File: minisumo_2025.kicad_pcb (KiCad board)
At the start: 4 copper layers, 62.4 x 98 mm, 139 parts, among them J1 USB_C Connector, J10 DISTANCE_R90, J11 DISTANCE_R, J12 DISTANCE_RF, J13 DISTANCE_L90, J14 DISTANCE_L, J15 LINE_LEFT, J16 DISTANCE_LF, J3 START_MODULE, J4 MOTOR1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

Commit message: routing
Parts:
- removed the C10 at (129.6, 46.6)
- removed the C10 at (161.6, 39.9)
- removed the C11 at (129.0, 55.9)
- removed the C11 at (162.3, 49.5)
- removed the C13 at (157.7, 59.7)
- removed the C13 at (123.5, 66.2)
- removed the C3 at (159.8, 58.8)
- removed the C3 at (126.0, 65.3)
- removed the C4 at (156.9, 46.6)
- removed the C4 at (124.8, 53.2)
- removed the C5 at (159.1, 49.5)
- removed the C5 at (125.3, 55.9)
- removed the C8 at (161.6, 43.2)
- removed the C8 at (129.6, 53.2)
- removed the C9 at (161.6, 46.7)
- removed the C9 at (129.6, 49.9)
- removed the L1 at (130.7, 61.0)
- removed the L1 at (165.3, 55.0)
- removed the R4 at (119.1, 62.7)
- removed the R4 at (154.0, 56.5)
- removed the R5 at (120.7, 62.8)
- removed the R5 at (155.1, 56.5)
- removed the U1 at (124.2, 61.0)
- removed the U1 at (158.4, 54.3)
- added C10: 47uF, Capacitor_SMD:C_1210_3225Metric, F.Cu at (125.4, 47.6)
- added C11: 100nF, Capacitor_SMD:C_0603_1608Metric, F.Cu at (126.4, 57.1)
- added C13: 1uF, Capacitor_SMD:C_0603_1608Metric, F.Cu at (121.7, 67.2)
- added C3: 0.1uF, Capacitor_SMD:C_0603_1608Metric, F.Cu at (124.0, 66.5)
- added C4: 10uF, Capacitor_SMD:C_1210_3225Metric, F.Cu at (120.7, 54.3)
- added C5: 220nF, Capacitor_SMD:C_0805_2012Metric, F.Cu at (123.1, 57.2)
- added C8: 47uF, Capacitor_SMD:C_1210_3225Metric, F.Cu at (125.4, 54.3)
- added C9: 47uF, Capacitor_SMD:C_1210_3225Metric, F.Cu at (125.4, 50.9)
- added L1: 10uH, 27mOhm, footprints:IND_XAL6060-103MEC, F.Cu at (129.1, 62.5)
- added R4: 100k, Resistor_SMD:R_0603_1608Metric, F.Cu at (117.2, 63.9)
- added R5: 22.1k, Resistor_SMD:R_0603_1608Metric, F.Cu at (118.7, 63.9)
- added U1: LMR33630ADDAR, footprints:DDA0008J, F.Cu at (122.3, 62.0)
- TP13: value GPIO48 -> GPIO17
- moved D2 79.0 mm to (109.7, 124.3)
- moved R6 78.8 mm to (113.8, 124.2)
- moved D1 18.5 mm to (131.9, 47.3), turned to 180 degrees
- moved R22 10.8 mm to (115.1, 70.2), turned to 90 degrees
- moved C15 9.33 mm to (118.4, 47.4), turned to -90 degrees
- moved R23 8.91 mm to (117.0, 120.2), turned to 90 degrees
- moved R24 8.87 mm to (117.2, 117.1), turned to 90 degrees
- moved R2 7.85 mm to (159.6, 76.2)
- moved R32 6.78 mm to (115.5, 120.2), turned to -90 degrees
- moved R21 6.74 mm to (115.1, 67.2), turned to 90 degrees
- moved D18 6.53 mm to (115.5, 117.1), turned to -90 degrees
- moved U4 3.65 mm to (115.4, 47.2), turned to 180 degrees
- moved C14 2.49 mm to (112.4, 47.4), turned to -90 degrees
- moved D17 0.98 mm to (109.5, 65.1)
- moved R31 0.98 mm to (112.5, 65.1)
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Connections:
- J8 pad 3: /GPIO12 -> /GPIO48
- J8 pad 4: /GPIO11 -> /GPIO47
- J8 pad 5: /GPIO10 -> /GPIO21
- R19 pad 1: /GPIO14 -> /GPIO38
- TP13 pad 1: /GPIO48 -> /GPIO17
- U3 pad 17: /DISTANCE_INTR -> /GPIO9
- U3 pad 22: /GPIO14 -> /DISTANCE_INTR
- U3 pad 4: /DISTANCE_L90 -> /DISTANCE_R90
- U3 pad 5: /DISTANCE_L -> /DISTANCE_R
- U3 pad 6: /DISTANCE_LF -> /DISTANCE_RF
- U3 pad 7: /DISTANCE_RF -> /DISTANCE_LF
- U3 pad 8: /DISTANCE_R -> /DISTANCE_L
- U3 pad 9: /DISTANCE_R90 -> /DISTANCE_L90
- U6 pad 1: /GPIO17 -> /GPIO10
- U6 pad 2: /GPIO21 -> /GPIO9
- U7 pad 1: /GPIO47 -> /GPIO12
- U7 pad 2: /GPIO38 -> /GPIO11
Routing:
- net /GPIO48: track 0.00 -> 40.3 mm
- net /GPIO21: track 11.7 -> 44.2 mm
- net /GPIO10: track 43.0 -> 14.1 mm
- net /GPIO47: track 18.2 -> 42.4 mm
- net /GPIO11: track 41.2 -> 19.6 mm
- net /GPIO12: track 39.2 -> 19.6 mm
- net /GPIO9: track 0.00 -> 12.8 mm
- net /GPIO17: track 12.7 -> 25.3 mm, vias 0 -> 2
- net /INV_2: track 50.9 -> 38.5 mm
- net /GPIO18: track 56.4 -> 45.7 mm
- net GND: track 21.7 -> 29.3 mm, vias 56 -> 95
- net +5V: track 8.18 -> 12.3 mm, vias 0 -> 2
- net /GPIO8: track 49.6 -> 52.8 mm
- net /DISTANCE_R: track 30.9 -> 33.2 mm
- net /DISTANCE_R90: track 33.0 -> 34.9 mm
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- added copper zone on In2.Cu, net +3V3
- added copper zone on In2.Cu, net +5V
- added copper zone on B.Cu, net /MOTOR2_B
- added copper zone on F.Cu, net /MOTOR2_B
- added copper zone on F.Cu, net GND
- removed copper zone on B.Cu, net GND

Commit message: layout done
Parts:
- added C16: 0.1uF, Capacitor_SMD:C_0603_1608Metric, F.Cu at (155.0, 72.0)
- moved C31 12.7 mm to (140.9, 111.7)
- moved R2 8.39 mm to (152.0, 79.7)
- moved R23 8.00 mm to (109.2, 121.8), turned to 180 degrees
- moved R22 7.78 mm to (109.2, 65.1), turned to 0 degrees
- moved D17 7.57 mm to (115.1, 70.1), turned to 90 degrees
- moved R24 6.82 mm to (112.2, 121.8), turned to 180 degrees
- moved R13 5.34 mm to (126.3, 92.6)
- moved R15 5.33 mm to (126.5, 106.6)
- moved R3 4.67 mm to (158.0, 69.0), turned to 180 degrees
- moved C27 4.48 mm to (135.6, 96.8), turned to -90 degrees
- moved R21 3.56 mm to (112.2, 65.1), turned to 0 degrees
- moved R31 3.33 mm to (115.1, 67.1), turned to -90 degrees
- moved R16 3.04 mm to (136.5, 94.0), turned to 180 degrees
- moved R29 1.50 mm to (123.7, 100.3)
- moved R6 1.13 mm to (112.7, 124.3)
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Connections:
- U1 pad V: (no net) -> GND
- U3 pad 4: /DISTANCE_R90 -> /DISTANCE_L90
- U3 pad 5: /DISTANCE_R -> /DISTANCE_LF
- U3 pad 6: /DISTANCE_RF -> /DISTANCE_L
- U3 pad 7: /DISTANCE_LF -> /DISTANCE_R
- U3 pad 8: /DISTANCE_L -> /DISTANCE_R90
- U3 pad 9: /DISTANCE_L90 -> /DISTANCE_RF
- U5 pad 1: /DISTANCE_L90 -> /DISTANCE_RF
- U5 pad 13: /DISTANCE_R90_OUT -> /DISTANCE_L90_OUT
- U5 pad 14: /DISTANCE_R_OUT -> /DISTANCE_LF_OUT
- U5 pad 15: /DISTANCE_RF_OUT -> /DISTANCE_L_OUT
- U5 pad 17: /DISTANCE_LF_OUT -> /DISTANCE_R_OUT
- U5 pad 18: /DISTANCE_L_OUT -> /DISTANCE_R90_OUT
- U5 pad 20: /DISTANCE_L90_OUT -> /DISTANCE_RF_OUT
- U5 pad 3: /DISTANCE_L -> /DISTANCE_R90
- U5 pad 4: /DISTANCE_LF -> /DISTANCE_R
- U5 pad 6: /DISTANCE_RF -> /DISTANCE_L
- U5 pad 7: /DISTANCE_R -> /DISTANCE_LF
- U5 pad 8: /DISTANCE_R90 -> /DISTANCE_L90
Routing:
- net +3V3: track 6.52 -> 78.5 mm, vias 0 -> 19
- net GND: track 29.3 -> 93.8 mm, vias 95 -> 142
- net +BATT: track 10.7 -> 69.9 mm, vias 24 -> 20
- net /ESP_EN: track 7.50 -> 47.3 mm, vias 0 -> 2
- net /SLEW_1: track 6.29 -> 30.5 mm, vias 0 -> 2
- net Net-(D1-A): track 3.27 -> 22.0 mm
- net (no net): track 0.00 -> 18.0 mm
- net +5V: track 12.3 -> 29.0 mm, vias 2 -> 12
- net /GPIO8: track 52.8 -> 65.4 mm, vias 1 -> 2
- net Net-(D3-A): track 0.00 -> 12.2 mm
- net /GPIO18: track 45.7 -> 56.7 mm, vias 1 -> 2
- net /LINE_LEFT_OUT: track 0.00 -> 9.88 mm
- net Net-(U6-~{SF}): track 0.00 -> 9.62 mm, vias 0 -> 2
- net Net-(J1-CC2): track 0.00 -> 9.39 mm
- net /DISTANCE_L90: track 25.5 -> 34.7 mm
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- added copper zone on F.Cu, net +5V
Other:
- board text added: "- dimensiuni componente mai mari de 0603 ✅ - thermal relief-uri pe ground ✅ - condensatori de mai multe valori pe batt input ✅ - valori VOLTAGE condensatori x3 mai mari - piese corecte - spatiere mai mare intre componente - D1 - low, D2 - high, SLEW - floating, INV - floating, FB - rezistenta la GND ✅ - pad-urile de breakout sa fie la 3v3, fara rezistente - le am scos momentan ✅ - leduri mai puti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"
- board text removed: "- dimensiuni componente mai mari de 0603 - thermal relief-uri pe ground - condensatori de mai multe valori pe batt input ✅ - valori VOLTAGE condensatori x3 mai mari - piese corecte - spatiere mai mare intre componente - D1 - low, D2 - high, SLEW - floating, INV - floating, FB - rezistenta la GND ✅ - pad-urile de breakout sa fie la 3v3, fara rezistente - le am scos momentan - leduri mai putin pute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"

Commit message: more changes
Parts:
- moved U2 0.94 mm to (153.3, 74.7)
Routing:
- net /D_P: track 6.54 -> 2.94 mm
- net /D_N: track 5.84 -> 2.93 mm
- net GND: track 93.8 -> 95.0 mm, vias 142 -> 152
- net /D+: track 12.2 -> 13.1 mm
- net Net-(D1-A): vias 2 -> 3
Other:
- board text added: "-"

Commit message: final layout
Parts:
- removed D1: D_Schottky_Small, Diode_SMD:D_SOD-123
- added C17: 0.1uF, Capacitor_SMD:C_0603_1608Metric, F.Cu at (155.0, 79.3)
- added FB1: FerriteBead_Small, Capacitor_SMD:C_0805_2012Metric, F.Cu at (154.1, 76.8)
- added Q1: Si2371EDS, Package_TO_SOT_SMD:SOT-23, F.Cu at (132.3, 48.5)
- C11, C26: value 100nF -> 0.1uF
- D5: value 8.2V -> 8V
- R17: value 412 -> 7k5
- R18: value 300 -> 5k5
- R19: value 68 -> 1k
- R20, R26, R27, R28, R29, R30, R31, R32: value ? -> 3k3
- R25: value 200 -> 3k3
- moved C26 25.4 mm to (153.1, 79.3), turned to -90 degrees
- moved R2 13.8 mm to (160.8, 69.1), turned to 0 degrees
- moved C6 4.86 mm to (153.1, 82.3), turned to -90 degrees
- moved D3 2.10 mm to (156.2, 82.0), turned to 180 degrees
- moved U2 0.95 mm to (154.2, 74.7)
- moved R3 0.63 mm to (157.4, 69.1)
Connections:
- C16 pad 1: Net-(D3-A) -> Net-(C16-Pad1)
- C26 pad 1: +BATT -> /VBUS
- C6 pad 1: Net-(D3-A) -> /VBUS
- D3 pad 2: Net-(D3-A) -> /VBUS
- J1 pad A4: Net-(D3-A) -> Net-(C16-Pad1)
- J1 pad A9: Net-(D3-A) -> Net-(C16-Pad1)
- J1 pad B4: Net-(D3-A) -> Net-(C16-Pad1)
- J1 pad B9: Net-(D3-A) -> Net-(C16-Pad1)
- U2 pad 5: +5V -> /VBUS
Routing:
- net /VBUS: track 0.00 -> 67.6 mm, vias 0 -> 3
- net Net-(C16-Pad1): track 0.00 -> 13.0 mm
- net Net-(D3-A): track 12.2 -> 0.00 mm
- net GND: track 95.0 -> 97.8 mm, vias 152 -> 133
- net Net-(J1-CC1): track 7.18 -> 9.80 mm, vias 0 -> 2
- net /D_N: track 2.93 -> 4.58 mm
- net /D_P: track 2.94 -> 4.58 mm
- net /DISTANCE_R: track 30.5 -> 29.2 mm
- net +5V: track 28.7 -> 27.6 mm, vias 12 -> 9
- net /DISTANCE_LF: track 33.2 -> 33.9 mm
- net Net-(J1-CC2): track 9.39 -> 8.74 mm
- net /D+: track 13.1 -> 13.6 mm
- net /D-: track 11.9 -> 12.4 mm

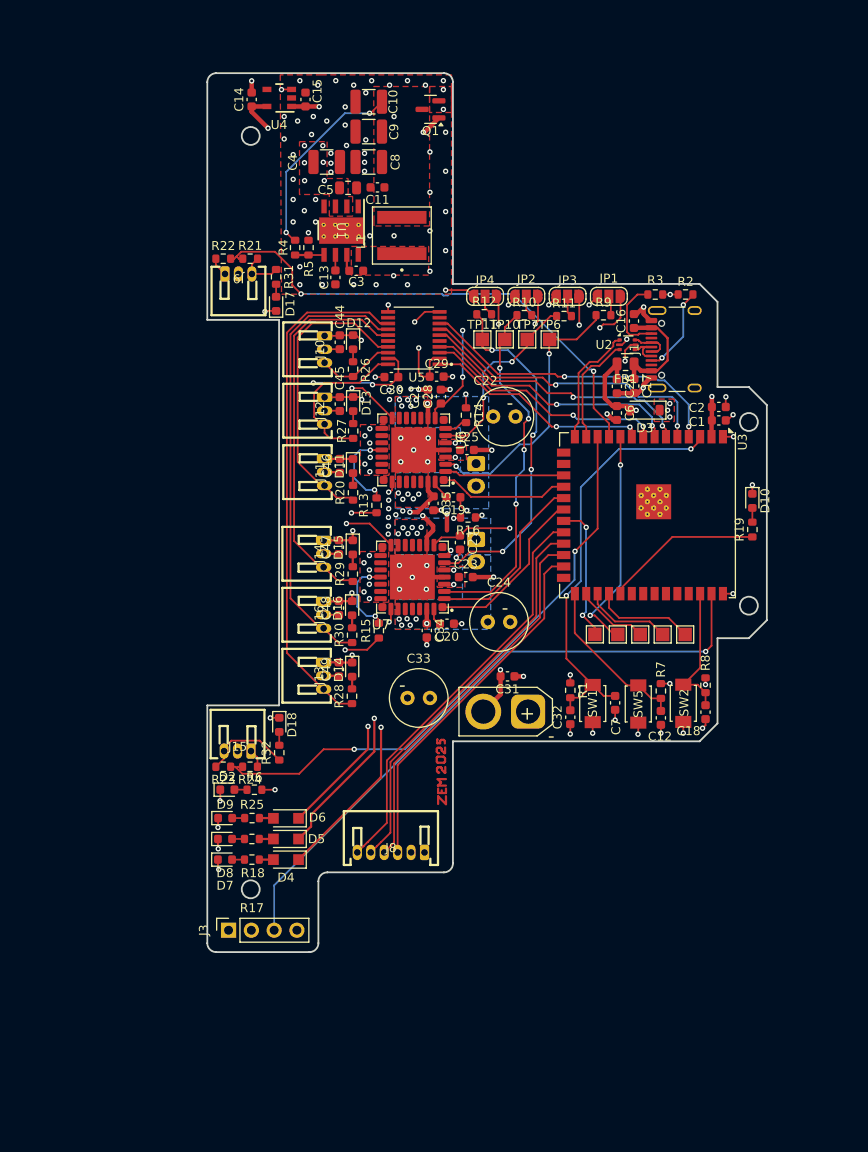
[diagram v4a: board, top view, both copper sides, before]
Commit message: silksreen and bom
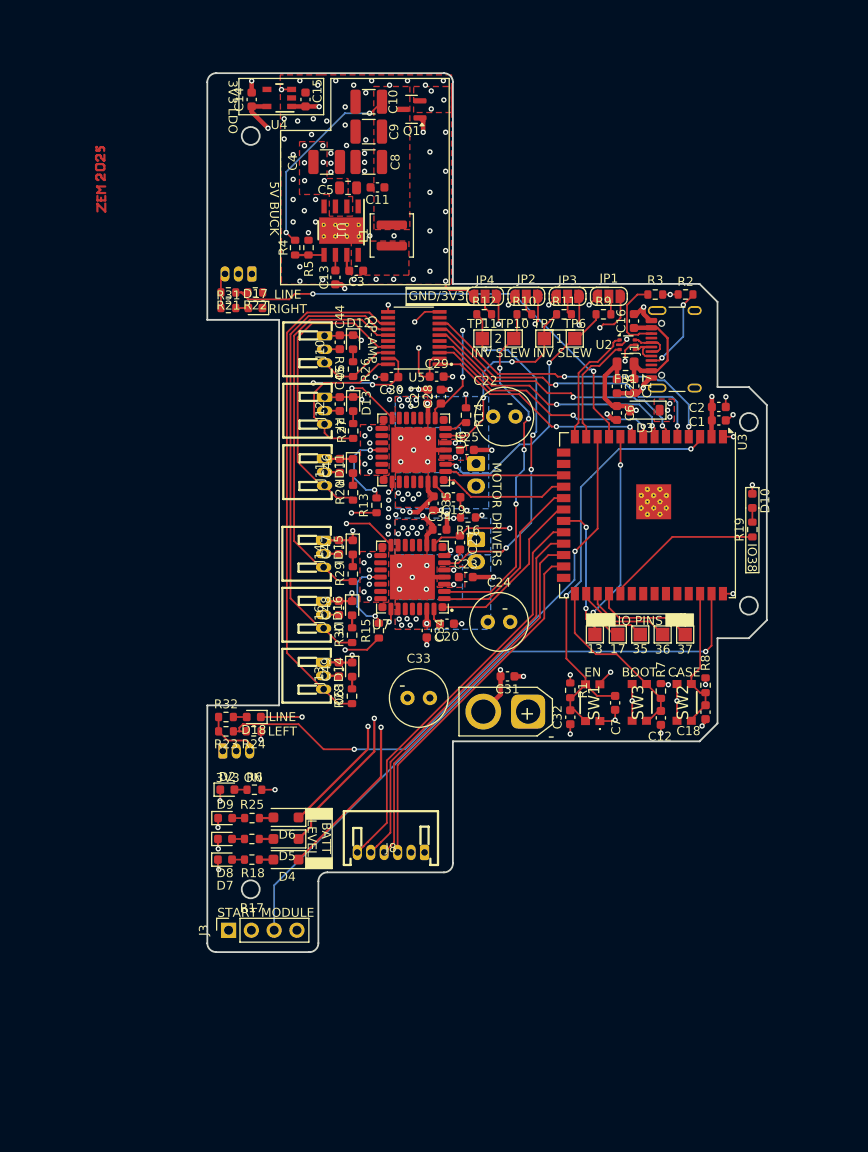
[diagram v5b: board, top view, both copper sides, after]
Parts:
- removed SW5: BOOT, footprints:SW_TS-1088-AR02016
- added C34: 0.1uF, Capacitor_SMD:C_0603_1608Metric, F.Cu at (133.3, 95.3)
- added SW3: BOOT, footprints:435441019830, F.Cu at (155.6, 114.6)
- C21, C23, C25, C27, C28, C44, C45, C46, C47, C48, C49: value 100nF -> 0.1uF
- C22, C24: value 100uF -> 100uF - low ESR
- D10: value 2Vf, 20mA, RED -> LED_Small
- D2, D7, D8, D9: value 2Vf, 20mA, RED -> 1.95Vf, 20mA, RED
- D4: footprint Diode_SMD:Nexperia_CFP3_SOD-123W -> Diode_SMD:D_SOD-123F
- D5: value 8V -> 8.2V; footprint Diode_SMD:Nexperia_CFP3_SOD-123W -> Diode_SMD:D_SOD-123F
- D6: value 6V -> 6.2V; footprint Diode_SMD:Nexperia_CFP3_SOD-123W -> Diode_SMD:D_SOD-123F
- J15, J9: moved to B.Cu
- L1: value 10uH, 27mOhm -> 8.2uH, 21mOhm; footprint footprints:IND_XAL6060-103MEC -> Inductor_SMD:L_Coilcraft_XAL4040-XXX
- R17: value 7k5 -> 5k
- R18: value 5k5 -> 3k74
- R22, R24: value 3.3k -> 3k3
- R25: value 3k3 -> 2k
- R5: value 22.1k -> 24k9
- R6: value 68 -> 1k
- SW1, SW2: footprint footprints:SW_TS-1088-AR02016 -> footprints:435441019830
- moved R32 7.15 mm to (109.5, 116.2), turned to 0 degrees
- moved R31 6.36 mm to (109.8, 70.6), turned to 0 degrees
- moved R22 5.19 mm to (112.8, 68.9), turned to 180 degrees
- moved R21 4.48 mm to (109.8, 68.9), turned to 180 degrees
- moved R24 3.98 mm to (112.6, 117.8)
- moved R23 3.96 mm to (109.5, 117.8)
- moved D18 2.97 mm to (112.6, 116.2), turned to 180 degrees
- moved TP6 2.80 mm to (148.4, 74.0)
- moved D17 2.36 mm to (112.8, 70.6), turned to 180 degrees
- moved Q1 2.11 mm to (130.2, 48.5)
- moved TP7 1.90 mm to (145.0, 74.0)
- moved L1 1.12 mm to (128.0, 62.5)
- moved TP10 1.00 mm to (141.6, 74.0)
- moved R11 0.20 mm to (147.2, 71.3)
- moved J15 0.15 mm to (110.7, 116.8), turned to 0 degrees
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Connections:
- U1 pad V: GND -> (no net)
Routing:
- net GND: track 97.8 -> 107.0 mm, vias 133 -> 135
- net /GPIO18: track 56.3 -> 52.8 mm
- net /LINE_LEFT_OUT: track 9.88 -> 6.47 mm
- net /ESP_EN: track 47.3 -> 49.2 mm
- net /ESP_BOOT: track 18.3 -> 20.1 mm
- net /SLEW_1: track 30.5 -> 28.9 mm
- net /INV_1: track 21.4 -> 23.0 mm
- net /VBUS: track 67.6 -> 66.5 mm
- net /CASE: track 15.2 -> 16.2 mm
- net /LINE_RIGHT_OUT: track 4.87 -> 3.99 mm
- net /GPIO17: track 25.3 -> 24.7 mm
- net Net-(Q1-D): vias 3 -> 2
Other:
- board text added: "1"
- board text added: "13"
- board text added: "17"
- board text added: "2"
- board text added: "35"
- board text added: "36"
- board text added: "37"
- board text added: "3V3 LDO"
- board text added: "3V3 ON"
- board text added: "5V BUCK"
- board text added: "BATT LEVEL"
- board text added: "BOOT"
- board text added: "CASE"
- board text added: "EN"
- board text added: "GND/3V3"
- board text added: "INV"
- board text added: "IO PINS"
- board text added: "IO38"
- board text added: "L"
- board text added: "L90"
- board text added: "LF"
- board text added: "LINE LEFT"
- board text added: "LINE RIGHT"
- board text added: "MOTOR DRIVERS"
- board text added: "OP-AMP"
- board text added: "R"
- board text added: "R90"
- board text added: "RF"
- board text added: "SLEW"
- board text added: "START MODULE"

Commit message: more changes
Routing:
- net GND: track 107.0 -> 107.7 mm
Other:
- board text added: "GND/PIN/3V3"
- board text removed: "GND/3V3"

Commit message: testing
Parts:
- C34: value 100nF -> 0.1uF
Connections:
- net /ESP_BOOT renamed /ESP32/ESP_BOOT
- net /ESP_EN renamed /ESP32/ESP_EN
- C18 pad 1: /CASE -> /ESP32/CASE
- R8 pad 2: /CASE -> /ESP32/CASE
- SW2 pad 2: /CASE -> /ESP32/CASE
- SW2 pad 3: /CASE -> /ESP32/CASE
- U3 pad 10: /GPIO17 -> /ESP32/GPIO17
- U3 pad 11: /GPIO18 -> /ESP32/GPIO18
- U3 pad 12: /GPIO8 -> /ESP32/GPIO8
- U3 pad 13: /D- -> /ESP32/D-
- U3 pad 14: /D+ -> /ESP32/D+
- U3 pad 17: /GPIO9 -> /ESP32/GPIO9
- U3 pad 18: /GPIO10 -> /ESP32/GPIO10
- U3 pad 19: /GPIO11 -> /ESP32/GPIO11
- U3 pad 20: /GPIO12 -> /ESP32/GPIO12
- U3 pad 21: /GPIO13 -> /ESP32/GPIO13
- U3 pad 22: /DISTANCE_INTR -> /ESP32/GPIO14
- U3 pad 23: /GPIO21 -> /ESP32/GPIO21
- U3 pad 24: /GPIO47 -> /ESP32/GPIO47
- U3 pad 25: /GPIO48 -> /ESP32/GPIO48
- U3 pad 28: /GPIO35 -> /ESP32/GPIO35
- U3 pad 29: /GPIO36 -> /ESP32/GPIO36
- U3 pad 30: /GPIO37 -> /ESP32/GPIO37
- U3 pad 31: /GPIO38 -> /ESP32/GPIO38
- U3 pad 38: /CASE -> /ESP32/GPIO2
- U3 pad 39: /GPIO1 -> /ESP32/GPIO1
- U3 pad 4: /DISTANCE_L90 -> /ESP32/GPIO4
- U3 pad 5: /DISTANCE_LF -> /ESP32/GPIO5
- U3 pad 6: /DISTANCE_L -> /ESP32/GPIO6
- U3 pad 7: /DISTANCE_R -> /ESP32/GPIO7
- U3 pad 8: /DISTANCE_R90 -> /ESP32/GPIO15
- U3 pad 9: /DISTANCE_RF -> /ESP32/GPIO16
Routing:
- net /CASE: track 16.2 -> 0.00 mm
- net (no net): track 18.0 -> 34.2 mm
